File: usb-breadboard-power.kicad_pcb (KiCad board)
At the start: 2 copper layers, 53 x 25.7 mm, 48 parts, among them J1 USB_C_Receptacle_PowerOnly_6P, J2 Conn_02x02, J3 Conn_02x02, J4 Conn_01x03, Q1 Q_PMOS_GSD, Q2 Q_PMOS_GSD, SW1 SW_DIP_x03, U1 CYPD3177, U2 BD33FC0FP, U3 LM339

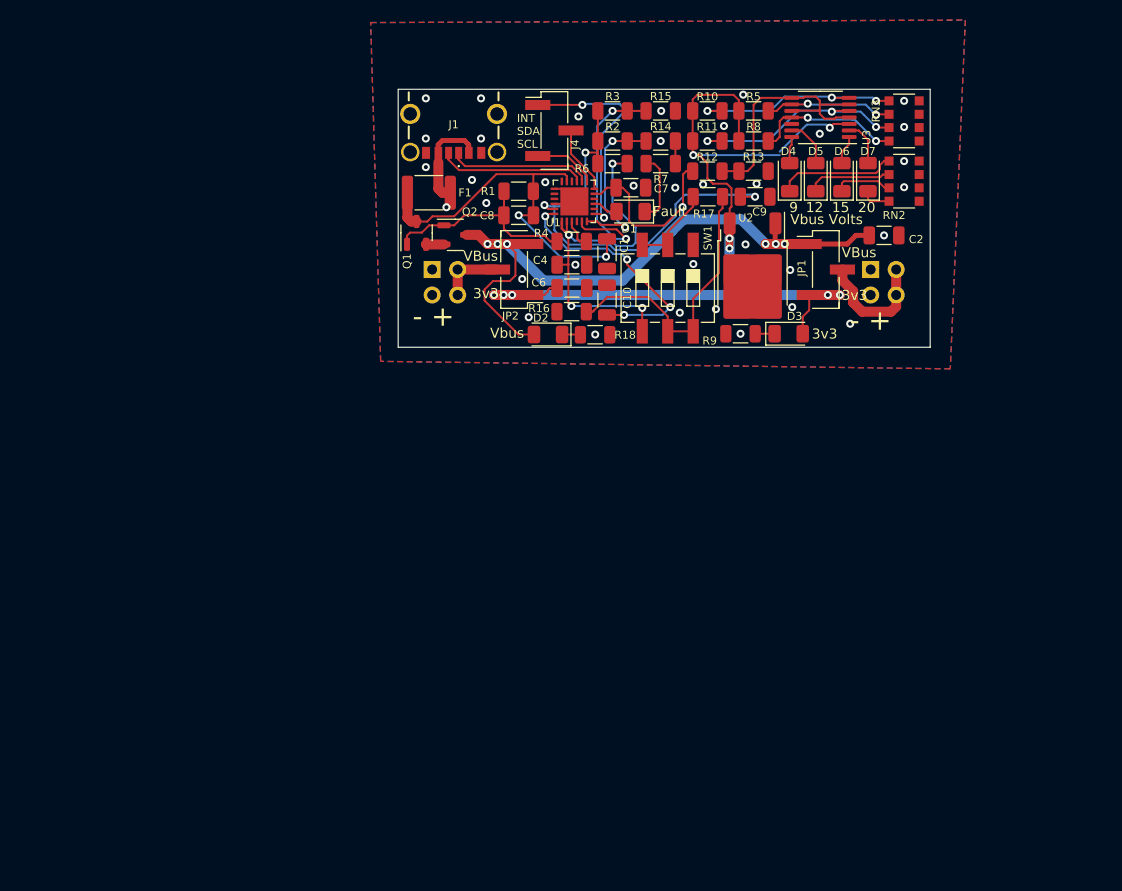
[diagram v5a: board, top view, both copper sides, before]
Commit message: Fixed switching reg layout
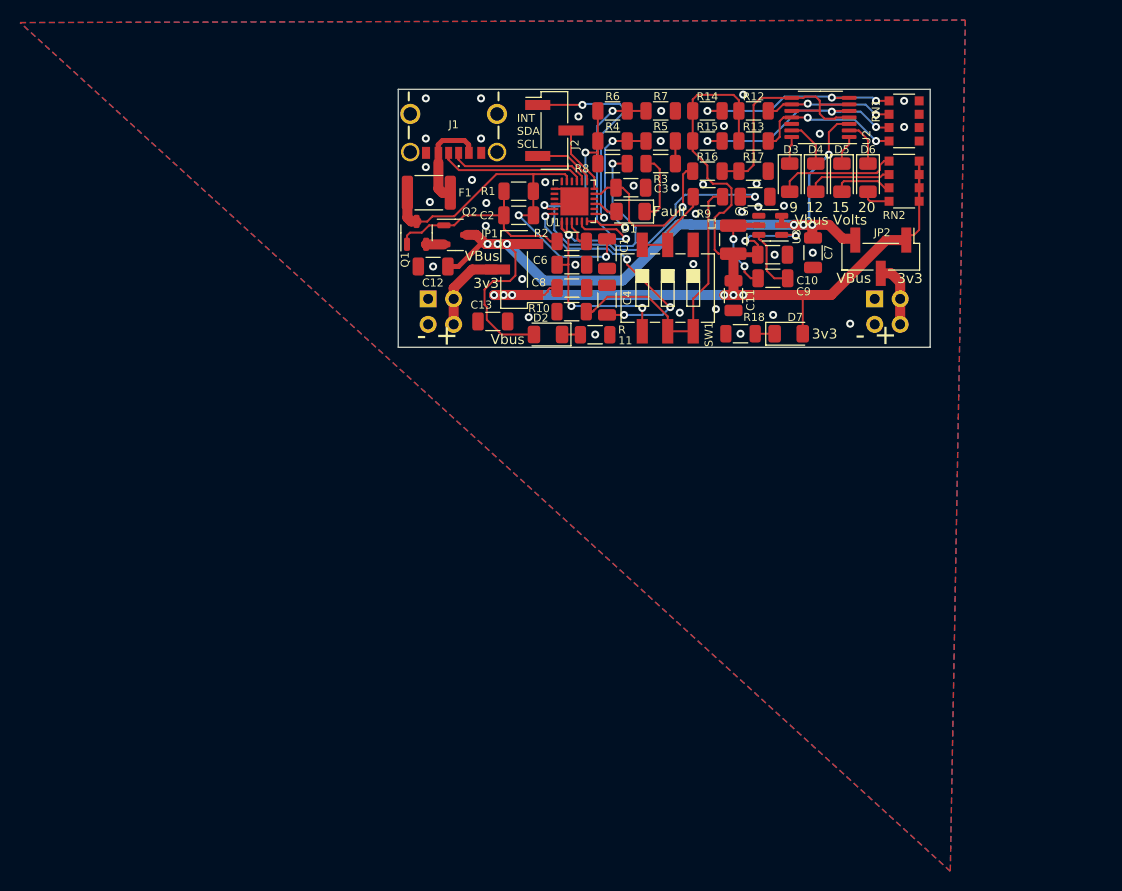
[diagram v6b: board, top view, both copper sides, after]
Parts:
- removed the U2 at (119.3, 102.0)
- added C10: 10u, Capacitor_SMD:C_1206_3216Metric, F.Cu at (121.3, 100.1)
- added C11: 10u, Capacitor_SMD:C_1206_3216Metric, F.Cu at (117.4, 104.2)
- added C12: 10u, Capacitor_SMD:C_1206_3216Metric, F.Cu at (87.5, 101.3)
- added C13: 10u, Capacitor_SMD:C_1206_3216Metric, F.Cu at (93.4, 106.8)
- added C9: 0.1u, Capacitor_SMD:C_1206_3216Metric, F.Cu at (121.3, 102.5)
- added L1: 4.7u, Inductor_SMD:L_1210_3225Metric, F.Cu at (117.4, 98.6)
- added U3: AP63203WU, Package_TO_SOT_SMD:TSOT-23-6, F.Cu at (121.1, 97.2)
- C3: renamed from C7; value 1u -> 10u
- C7: renamed from C2; value 1u -> 10u
- F1: value Fuse -> 2A
- R12: renamed from R5; value 0 -> 10.5k
- R13: renamed from R8; value 36.5k -> 49.9k
- R14: renamed from R10; value 73.2k -> 90.9k
- R15: renamed from R11; value 137k -> 162k
- R16: renamed from R12; value 536k -> 53.6k
- R17: renamed from R13; value 100k -> 10k
- moved C7 7.28 mm to (125.3, 99.9), turned to -90 degrees
- moved JP2 5.62 mm to (132.1, 100.3), turned to -90 degrees
- moved J3 2.95 mm to (87.0, 104.5)
- moved J4 2.95 mm to (131.5, 104.5)
- turned D3 to -90 degrees
- turned D4 to -90 degrees
- turned D5 to -90 degrees
- turned D6 to -90 degrees
- renumbered C8 to C2, C10 to C4, C9 to C5, C4 to C6, C6 to C8, D4 to D3, D5 to D4, D6 to D5, D7 to D6, D3 to D7, J4 to J2, J2 to J3, J3 to J4, JP2 to JP1, JP1 to JP2, R16 to R10, R18 to R11, R9 to R18, R4 to R2, R7 to R3, R2 to R4, R14 to R5, R3 to R6, R15 to R7, R6 to R8, R17 to R9, RN3 to RN1, U3 to U2
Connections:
- D3 pad 1: Net-(D4-K) -> Net-(D3-K)
- D3 pad 2: Net-(D4-A) -> Net-(D3-A)
- D4 pad 1: Net-(D5-K) -> Net-(D4-K)
- D4 pad 2: Net-(D5-A) -> Net-(D4-A)
- D5 pad 1: Net-(D6-K) -> Net-(D5-K)
- D5 pad 2: Net-(D6-A) -> Net-(D5-A)
- D6 pad 1: Net-(D7-K) (its old number) -> Net-(D6-K)
- D6 pad 2: Net-(D7-A) -> Net-(D6-A)
- JP2 pad 1: VBUS -> +3V3
- JP2 pad 3: +3V3 -> VBUS
- RN2 pad 1: GND -> +3V3
- RN2 pad 2: GND -> +3V3
- RN2 pad 3: GND -> +3V3
- RN2 pad 4: GND -> +3V3
- RN2 pad 5: Net-(D4-K) -> Net-(D3-A)
- RN2 pad 6: Net-(D5-K) -> Net-(D4-A)
- RN2 pad 7: Net-(D6-K) -> Net-(D5-A)
- RN2 pad 8: Net-(D7-K) (its old number) -> Net-(D6-A)
- U2 pad 1: Net-(D6-A) -> Net-(D5-K)
- U2 pad 13: Net-(D5-A) -> Net-(D4-K)
- U2 pad 14: Net-(D4-A) -> Net-(D3-K)
- U2 pad 2: Net-(D7-A) -> Net-(D6-K)
- U2 pad 3: +3V3 -> VBUS
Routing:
- net VBUS: track 89.0 -> 104.8 mm, vias 7 -> 8
- net Net-(D3-A): track 0.00 -> 12.0 mm
- net +3V3: track 99.9 -> 111.9 mm, vias 9 -> 8
- net Net-(U3-SW): track 0.00 -> 9.72 mm, vias 0 -> 2
- net Net-(D4-K): track 12.0 -> 4.80 mm
- net Net-(U3-BST): track 0.00 -> 6.34 mm
- net Net-(D4-A): track 2.68 -> 8.46 mm
- net Net-(D5-K): track 8.46 -> 2.90 mm
- net Net-(J4-Pin_3): track 12.3 -> 6.79 mm
- net Net-(D7-A): track 4.58 -> 0.00 mm
- net Net-(D7-K) (its old number): track 2.98 -> 0.00 mm
- net Net-(D3-K): track 0.00 -> 2.68 mm
- net Net-(J3-Pin_3): track 6.37 -> 8.61 mm
- net Net-(D6-K): track 5.86 -> 4.58 mm
- net Net-(D5-A): track 4.80 -> 5.86 mm
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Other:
- board text added: "11"
- board text added: "R"

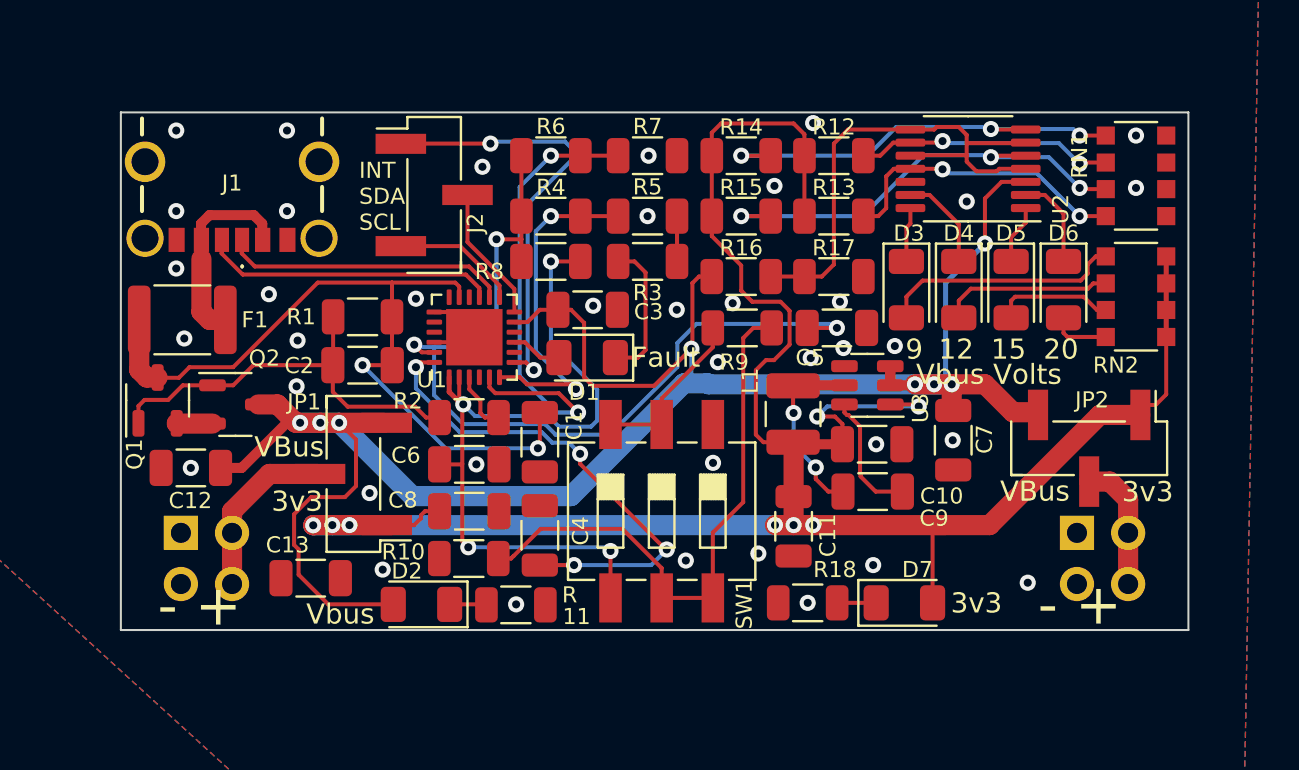
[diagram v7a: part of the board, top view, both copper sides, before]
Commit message: Fixed issues discovered while building first run
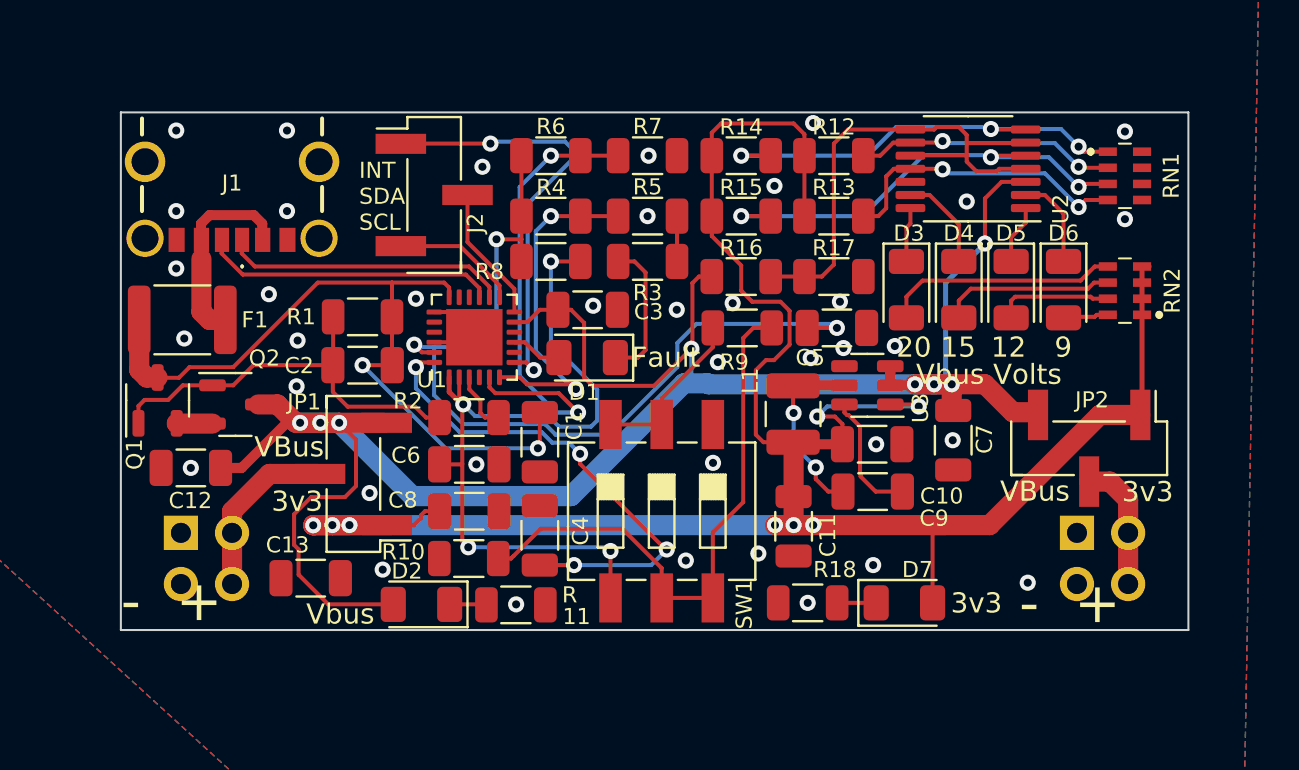
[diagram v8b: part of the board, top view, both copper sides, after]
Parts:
- J2: value Conn_01x03 -> DNP
- RN1, RN2: footprint Resistor_SMD:R_Array_Convex_4x1206 -> usb-breadboard:CAY16472J4LF
- moved RN2 0.63 mm to (133.8, 92.5), turned to 90 degrees
- moved RN1 0.55 mm to (133.8, 86.8), turned to -90 degrees
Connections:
- U1 pad 17: Net-(Q1-D) -> unconnected-(U1-D+-Pad17)
- U1 pad 18: (no net) -> Net-(Q1-D)
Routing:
- net +3V3: track 111.9 -> 111.3 mm
- net Net-(Q1-D): track 39.1 -> 38.5 mm
